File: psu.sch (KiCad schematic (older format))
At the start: 0 parts

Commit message: Start Rev A
The LT3081 does it all.
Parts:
- added C1: 0u1, symbol Device:C_Small
- added C2: 10u, symbol pspice:C
- added D?: LED_ALT, symbol Device:LED_ALT
- added J1: Screw_Terminal_01x02, symbol Connector:Screw_Terminal_01x02
- added J2: Conn_01x02, symbol Connector_Generic:Conn_01x02
- added MES1: Voltmeter_DC, symbol Device:Voltmeter_DC
- added R1: 2R8, symbol Device:R
- added R10: 22R, symbol Device:R
- added R2: 6R9, symbol Device:R
- added R3: 14R, symbol Device:R
- added R4: 28R, symbol Device:R
- added R5: 69R, symbol Device:R
- added R6: 139R, symbol Device:R
- added R7: 278R, symbol Device:R
- added R8: 5k, symbol Device:R
- added R9: 1k, symbol Device:R
- added R?: R, symbol Device:R
- added RV1: 500k, symbol Device:R_POT_US
- added RV2: 10k, symbol Device:R_POT_US
- added SW1, SW2, SW3: SW_SP4T, symbol psu-sch:SW_SP4T
- added TP1, TP3: TestPoint, symbol Connector:TestPoint
- added TP2: TestPoint_2Pole, symbol Connector:TestPoint_2Pole
- added U1: LT3081, symbol psu-sch:LT3081
- added U2: LM334M, Package_SO:SOIC-8_3.9x4.9mm_P1.27mm, symbol Reference_Current:LM334M
- added U? (x2): LM358, symbol Amplifier_Operational:LM358
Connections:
- net labels added: GND, Isense, TEMP, Vin, Vout
- wire segments 0 -> 119
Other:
- note added: "**"
- note added: "** Ceramic X5R or X7R"
- note added: "1 mA"
- note added: "1 mV/mA"
- note added: "1 mV/°C"
- note added: "10 mA"
- note added: "100 mA"
- note added: "2.5 mA"
- note added: "25 mA"
- note added: "5 mA"
- note added: "50 mA"
- note added: "Best values, not standard values\nWill maybe use potentiometers?"
- note added: "Binding posts"
- note added: "Coarse"
- note added: "Fine"
- note added: "SparkFun (PRT-14313)\nor similar 3-digit voltmeter\nDigikey: 1568-1700-ND"
- note added: "TODO: Properly drive current-limit indicator LED"
- note added: "TODO: Stabilize"

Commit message: Closer to final; need offset
Need to deal with input offset for current protection / regulation comparator. Add an adder before the comparator?
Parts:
- removed D?: LED_ALT, symbol Device:LED_ALT
- removed MES1: Voltmeter_DC, symbol Device:Voltmeter_DC
- removed R?: R, symbol Device:R
- removed SW3: SW_SP4T, symbol psu-sch:SW_SP4T
- removed U?: LM358, symbol Amplifier_Operational:LM358
- added D1, D2: LED_RED, symbol Device:LED_ALT
- added J2: Barrel_Jack, symbol Connector:Barrel_Jack
- added R1: 4k7, symbol Device:R
- added R10, R12: 1k, symbol Device:R
- added R13, R14: 220R, symbol Device:R
- added R9: 24k, symbol Device:R
- added R? (x2): R, symbol Device:R
- added R? (x2): Rm, symbol Device:R
- added R?: Rf/2, symbol Device:R
- added R?: Rf, symbol Device:R
- added TP2, TP4, TP5, TP6: TestPoint, symbol Connector:TestPoint
- added U1: LM4040DBZ-2.5, Package_TO_SOT_SMD:SOT-23, symbol Reference_Voltage:LM4040DBZ-2.5
- added unit 3 of U2
- added U3: LM358, symbol Amplifier_Operational:LM358
- added U5, U6: LM317L_TO92, Package_TO_SOT_THT:TO-92_Inline, symbol Regulator_Linear:LM317L_TO92
- added U?: LM324, symbol Amplifier_Operational:LM324
- gave numbers to parts that had none: 1
- renumbered J2 to J3, R8 to R15, R9 to R16, R10 to R17, R1 to R2, R2 to R3, R3 to R4, R4 to R5, R5 to R6, R6 to R7, R7 to R8, TP2 to TP7, U1 to U4, U2 to U7
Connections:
- net labels added: 2.5Vref
- wire segments 119 -> 166
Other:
- note added: "Best values, not standard values\nWill maybe use potentiometers?\nTODO: offset to provide correct current limit\ngiven offset from LM334"
- note added: "TODO: Offset"
- note removed: "Best values, not standard values\nWill maybe use potentiometers?"
- note removed: "SparkFun (PRT-14313)\nor similar 3-digit voltmeter\nDigikey: 1568-1700-ND"
- note removed: "TODO: Properly drive current-limit indicator LED"
- note removed: "TODO: Stabilize"
- moved on the sheet: C1, C2, J1, J3, R15, R16, R17, R2, R3, R4, R5, R6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

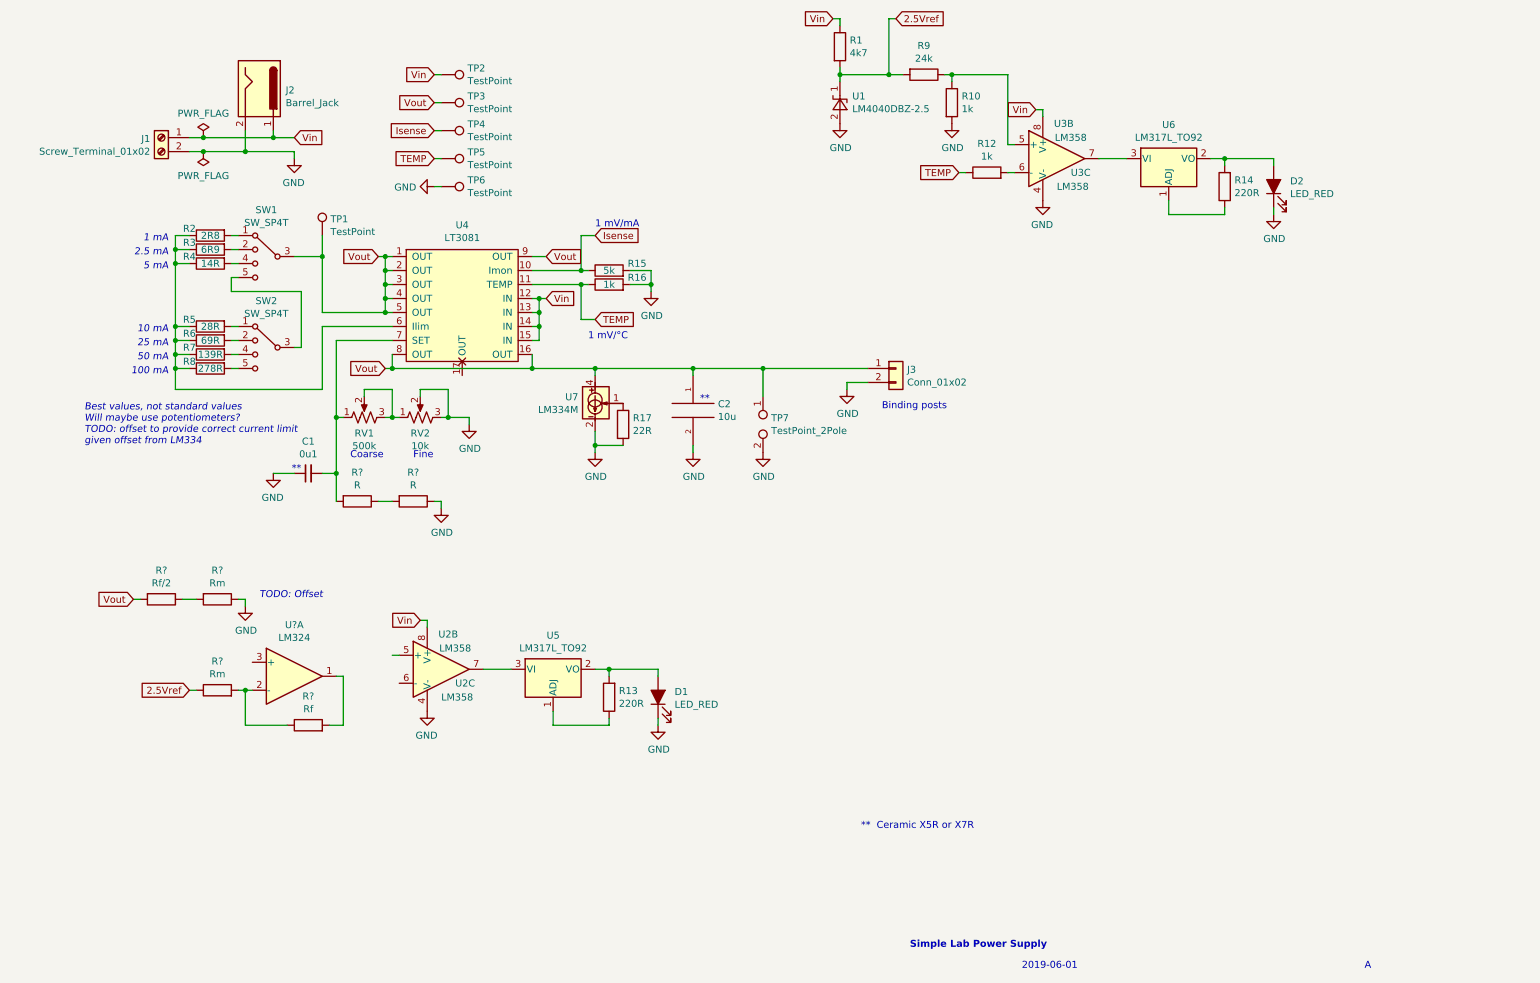
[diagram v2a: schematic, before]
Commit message: Rev A schematic finished!
May need to slightly tweak resistor values based on available stock.
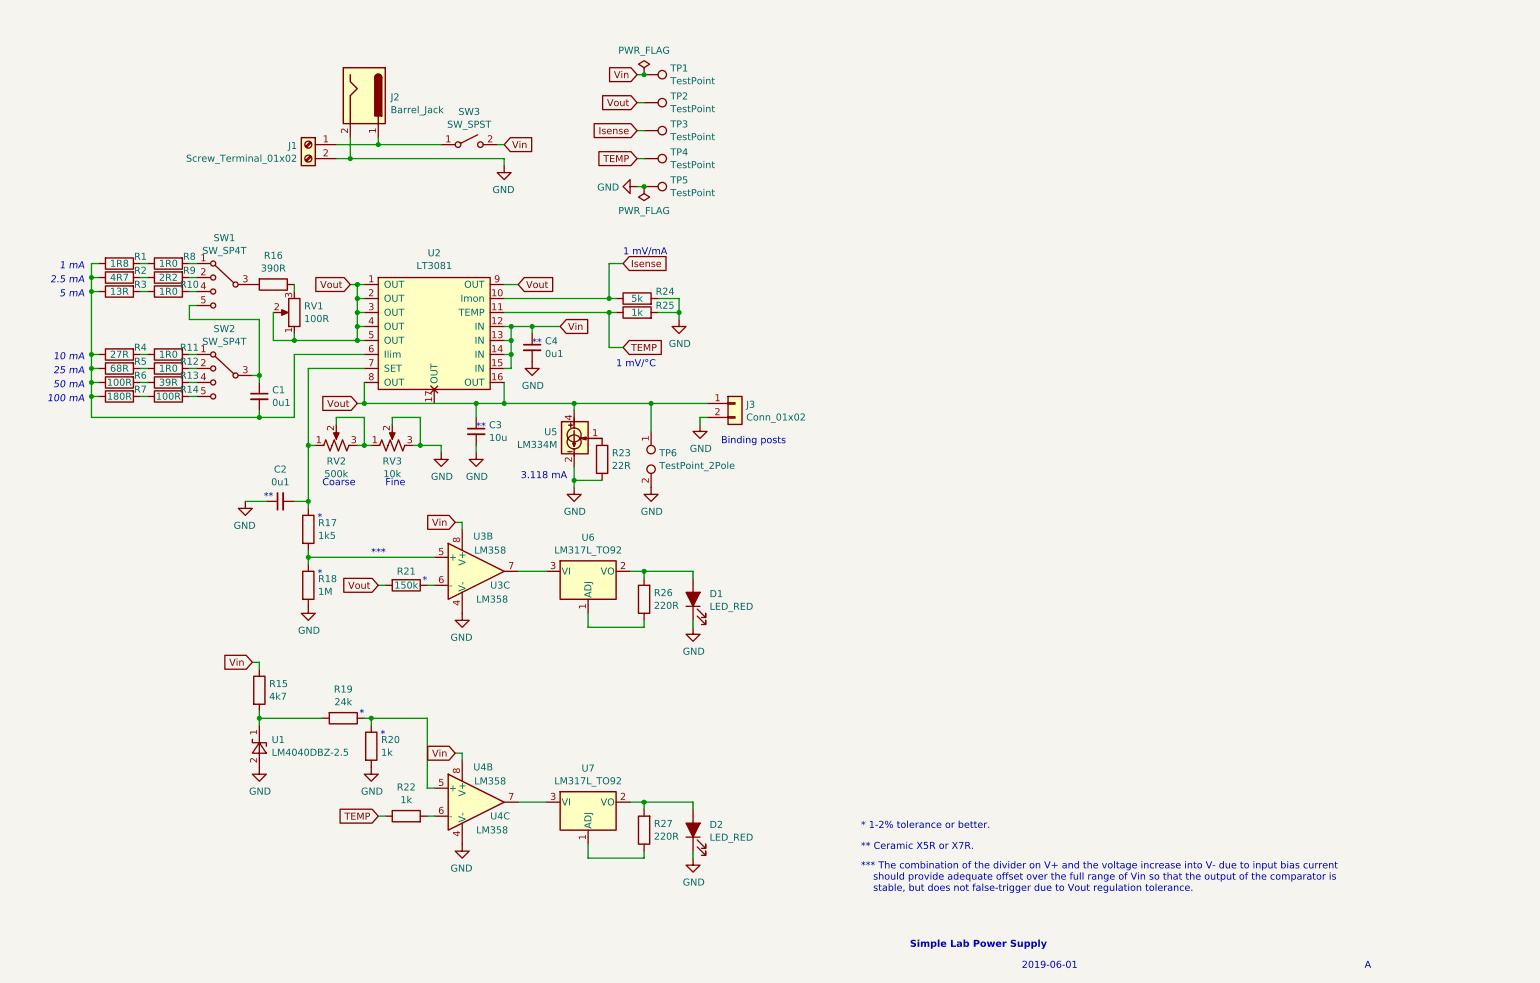
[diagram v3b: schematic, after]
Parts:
- removed C2: 10u, symbol pspice:C
- removed R? (x2): R, symbol Device:R
- removed R? (x2): Rm, symbol Device:R
- removed R?: Rf/2, symbol Device:R
- removed R?: Rf, symbol Device:R
- removed TP1: TestPoint, symbol Connector:TestPoint
- removed U?: LM324, symbol Amplifier_Operational:LM324
- added C1, C4: 0u1, symbol Device:C_Small
- added C3: 10u, symbol Device:C_Small
- added R1: 1R8, symbol Device:R
- added R10, R11, R12: 1R0, symbol Device:R
- added R16: 390R, symbol Device:R
- added R17: 1k5, symbol Device:R
- added R18: 1M, symbol Device:R
- added R2: 4R7, symbol Device:R
- added R21: 150k, symbol Device:R
- added R6: 100R, symbol Device:R
- added R7: 180R, symbol Device:R
- added RV1: 100R, symbol Device:R_POT
- added SW3: SW_SPST, symbol Switch:SW_SPST
- R13: renamed from R7; value 139R -> 39R
- R14: renamed from R8; value 278R -> 100R
- R3: renamed from R4; value 14R -> 13R
- R4: renamed from R5; value 28R -> 27R
- R5: renamed from R6; value 69R -> 68R
- R8: renamed from R2; value 2R8 -> 1R0
- R9: renamed from R3; value 6R9 -> 2R2
- renumbered C1 to C2, R1 to R15, R9 to R19, R10 to R20, R12 to R22, R17 to R23, R15 to R24, R16 to R25, R13 to R26, R14 to R27, RV1 to RV2, RV2 to RV3, TP2 to TP1, TP3 to TP2, TP4 to TP3, TP5 to TP4, TP6 to TP5, TP7 to TP6, U4 to U2, U2 to U3, U3 to U4, U7 to U5, U5 to U6, U6 to U7
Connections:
- net GND: now also C3.2, C4.2, R18.2
- net Vin: now also C4.1, SW3.2 (B); no longer J1.1 (Pin_1), J2.1
- net Vout: now also C3.1, R21.2, RV1.1, RV1.2; no longer SW1.3
- net at R3.1, R4.1, R5.1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: now also C1.2, R1.2, R2.1, R6.1, R7.1; no longer R13.1, R14.1, R8.1, R9.1
- net at C2.2, RV2.1, U2.7 (SET): now also R17.1
- net at SW1.4: now also R10.2; no longer R3.2
- net at SW1.5, SW2.3: now also C1.1
- net at SW2.1: now also R11.2; no longer R4.2
- net at SW2.2: now also R12.2; no longer R5.2
- net at U3.5 (+): now also R17.2, R18.1
- net at U3.6 (-): now also R21.1
- net 2.5Vref: no longer names the net of R15.2, R19.2, U1.1 (K)
- new net: R16.2, SW1.3
- new net: R1.1, R8.1
- new net: R2.2, R9.1
- new net: R10.1, R3.2
- new net: R11.1, R4.2
- new net: R12.1, R5.2
- new net: R13.1, R6.2
- new net: R14.1, R7.2
- new net: J1.1 (Pin_1), J2.1, SW3.1 (A)
- new net: R16.1, RV1.3
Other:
- note added: "*"
- note added: "* 1-2% tolerance or better."
- note added: "** Ceramic X5R or X7R."
- note added: "***"
- note added: "*** The combination of the divider on V+ and the voltage increase into V- due to input bias current\n should provide adequate offset over the full range of Vin so that the output of the comparator is\n stable, but does not false-trigger due to Vout regulation tolerance."
- note added: "3.118 mA"
- note removed: "** Ceramic X5R or X7R"
- note removed: "Best values, not standard values\nWill maybe use potentiometers?\nTODO: offset to provide correct current limit\ngiven offset from LM334"
- note removed: "TODO: Offset"
- moved on the sheet: C2, D1, D2, J1, J2, J3, R13, R14, R15, R19, R20, R22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

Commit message: Finalization of resistor values
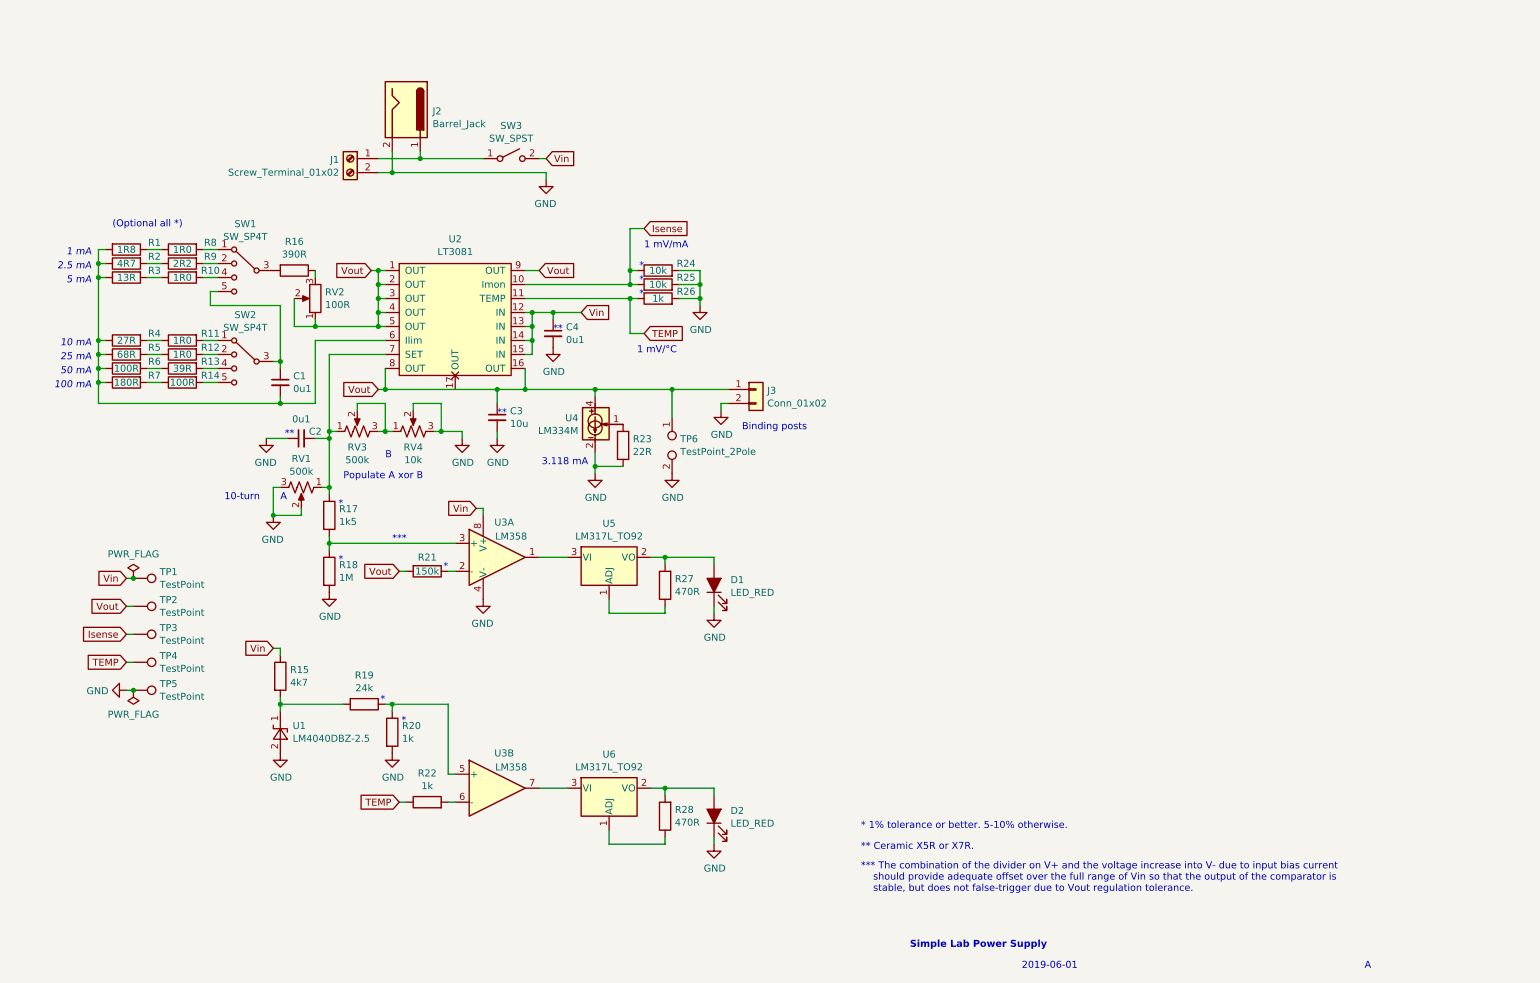
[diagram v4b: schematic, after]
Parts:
- removed U4: LM358, symbol Amplifier_Operational:LM358
- added R25: 10k, symbol Device:R
- added RV1: 500k, symbol Device:R_POT_US
- added unit 1 of U3
- R24: value 5k -> 10k
- R27: renamed from R26; value 220R -> 470R
- R28: renamed from R27; value 220R -> 470R
- renumbered R25 to R26, RV1 to RV2, RV2 to RV3, RV3 to RV4, U5 to U4, U6 to U5, U7 to U6
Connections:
- net GND: now also R25.2, RV1.2, RV1.3
- net Isense: now also R25.1
- net at C2.2, R17.1, RV3.1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: now also RV1.1
- net at U5.3 (VI): now also U3.1; no longer U3.7
- net at R17.2, R18.1: now also U3.3 (+); no longer U3.5 (+)
- net at U6.3 (VI): now also U3.7
- net at R21.1: now also U3.2 (-); no longer U3.6 (-)
- net at R19.1, R20.1: now also U3.5 (+)
- net at R22.2: now also U3.6 (-)
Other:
- note added: "(Optional all *)"
- note added: "* 1% tolerance or better. 5-10% otherwise."
- note added: "10-turn"
- note added: "B"
- note added: "Populate A xor B"
- note removed: "* 1-2% tolerance or better."
- note removed: "Coarse"
- note removed: "Fine"
- moved on the sheet: C1, C2, C3, C4, D1, D2, J1, J2, J3, R1, R10, R11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

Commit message: Most footprints entered
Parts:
- removed RV1: 500k, symbol Device:R_POT_US
- C1, C2, C4: footprint (none) -> Capacitor_THT:C_Disc_D5.0mm_W2.5mm_P2.50mm
- C3: footprint (none) -> Capacitor_SMD:C_1206_3216Metric_Pad1.42x1.75mm_HandSolder
- D1, D2: footprint (none) -> LED_THT:LED_D5.0mm
- J1: footprint (none) -> TerminalBlock_MetzConnect:TerminalBlock_MetzConnect_Type094_RT03502HBLU_1x02_P5.00mm_Horizontal
- J2: footprint (none) -> Connector_BarrelJack:BarrelJack_Horizontal
- R1, R10, R11, R12, R13, R14, R17, R18, R19, R2, R20, R21, R24, R25, R26, R3, R4, R5, R6, R7, R8, R9: footprint (none) -> Resistor_SMD:R_1206_3216Metric_Pad1.42x1.75mm_HandSolder
- R15, R16, R22, R23, R27, R28: footprint (none) -> Resistor_THT:R_Axial_DIN0207_L6.3mm_D2.5mm_P10.16mm_Horizontal
- RV1: renamed from RV2; footprint (none) -> Potentiometer_THT:Potentiometer_Piher_PC-16_Single_Horizontal
- RV2: renamed from RV3; footprint (none) -> Potentiometer_THT:Potentiometer_Piher_PC-16_Single_Horizontal
- RV3: renamed from RV4; footprint (none) -> Potentiometer_THT:Potentiometer_Piher_PC-16_Single_Horizontal
- TP1, TP2, TP3, TP4, TP5: footprint (none) -> TestPoint:TestPoint_Bridge_Pitch2.54mm_Drill1.3mm
- TP6: footprint (none) -> TestPoint:TestPoint_2Pads_Pitch5.08mm_Drill1.3mm
- U2: footprint (none) -> Package_SO:HTSSOP-16-1EP_4.4x5mm_P0.65mm_EP3.4x5mm_Mask3x3mm_ThermalVias
- U3: footprint (none) -> Package_SO:SOIC-8_3.9x4.9mm_P1.27mm
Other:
- note removed: "10-turn"
